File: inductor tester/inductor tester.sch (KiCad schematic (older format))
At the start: 39 parts, among them P101 I Sense, P102 Inductor Under Test, P103 V Sense, P104 10V_In, P105 0V_In, Q101 BC847, Q102 PSMN4R3-30BL, SW101 SW_PUSH, U102 LM555N

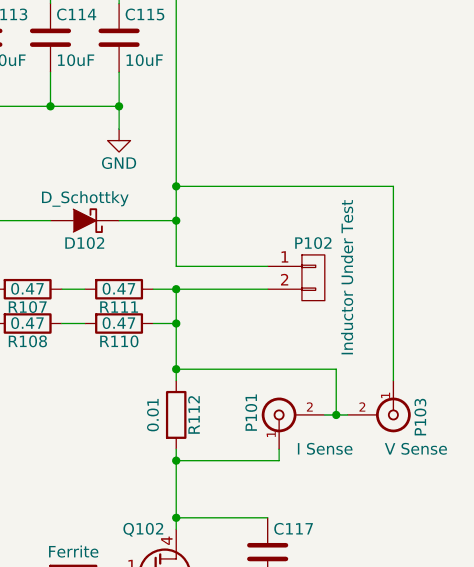
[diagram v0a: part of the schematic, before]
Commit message: Added notes on exporting, saved PCB as ordered.
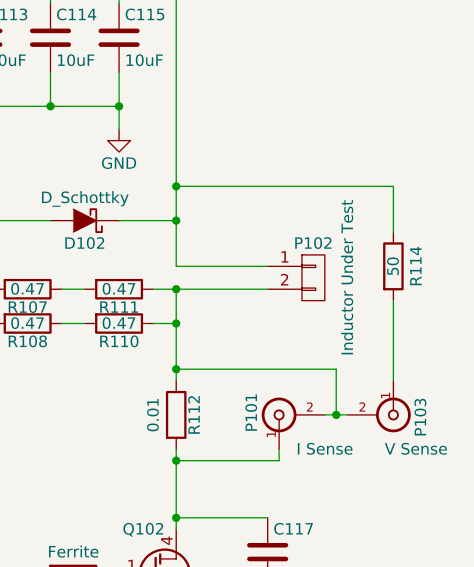
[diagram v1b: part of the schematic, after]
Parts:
- added R114: 50, Resistors_SMD:R_0805_HandSoldering, symbol R
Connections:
- net VCC: now also R114.1; no longer P103.1 (In)
- new net: P103.1 (In), R114.2
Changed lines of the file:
@@
 $EndComp
 $Comp
-L GND #PWR01
+L GND #PWR113
 U 1 1 571D57D3
 P 7350 5600
-F 0 "#PWR01" H 7350 5350 50  0001 C CNN
+F 0 "#PWR113" H 7350 5350 50  0001 C CNN
 F 1 "GND" H 7350 5450 50  0000 C CNN
 F 2 "" H 7350 5600 50  0000 C CNN
@@
 $EndComp
 $Comp
-L GND #PWR02
+L GND #PWR114
 U 1 1 571D8329
 P 8150 2800
-F 0 "#PWR02" H 8150 2550 50  0001 C CNN
+F 0 "#PWR114" H 8150 2550 50  0001 C CNN
 F 1 "GND" H 8150 2650 50  0000 C CNN
 F 2 "" H 8150 2800 50  0000 C CNN
@@
 $EndComp
 $Comp
-L GND #PWR03
+L GND #PWR102
 U 1 1 571DCF93
 P 4300 3800
-F 0 "#PWR03" H 4300 3550 50  0001 C CNN
+F 0 "#PWR102" H 4300 3550 50  0001 C CNN
 F 1 "GND" H 4300 3650 50  0000 C CNN
 F 2 "" H 4300 3800 50  0000 C CNN
@@
 $EndComp
 $Comp
-L GND #PWR04
+L GND #PWR110
 U 1 1 571DD8DF
 P 6500 5600
-F 0 "#PWR04" H 6500 5350 50  0001 C CNN
+F 0 "#PWR110" H 6500 5350 50  0001 C CNN
 F 1 "GND" H 6500 5450 50  0000 C CNN
 F 2 "" H 6500 5600 50  0000 C CNN
@@
 $EndComp
 $Comp
-L VCC #PWR05
+L VCC #PWR111
 U 1 1 571DF26F
 P 6950 3050
-F 0 "#PWR05" H 6950 2900 50  0001 C CNN
+F 0 "#PWR111" H 6950 2900 50  0001 C CNN
 F 1 "VCC" H 6950 3200 50  0000 C CNN
 F 2 "" H 6950 3050 50  0000 C CNN
@@
 $EndComp
 $Comp
-L VCC #PWR06
+L VCC #PWR107
 U 1 1 571DF3CD
 P 5150 3050
-F 0 "#PWR06" H 5150 2900 50  0001 C CNN
+F 0 "#PWR107" H 5150 2900 50  0001 C CNN
 F 1 "VCC" H 5150 3200 50  0000 C CNN
 F 2 "" H 5150 3050 50  0000 C CNN
@@
 $EndComp
 $Comp
-L VCC #PWR07
+L VCC #PWR105
 U 1 1 571DF44D
 P 4800 4600
-F 0 "#PWR07" H 4800 4450 50  0001 C CNN
+F 0 "#PWR105" H 4800 4450 50  0001 C CNN
 F 1 "VCC" H 4800 4750 50  0000 C CNN
 F 2 "" H 4800 4600 50  0000 C CNN
@@
 $EndComp
 $Comp
-L VCC #PWR08
+L VCC #PWR109
 U 1 1 571DF73B
 P 6500 4500
-F 0 "#PWR08" H 6500 4350 50  0001 C CNN
+F 0 "#PWR109" H 6500 4350 50  0001 C CNN
 F 1 "VCC" H 6500 4650 50  0000 C CNN
 F 2 "" H 6500 4500 50  0000 C CNN
@@
 Wire Wire Line
 	9100 3850 9100 4050
-Wire Wire Line
-	9350 3050 9350 3900
 Wire Wire Line
 	8800 4800 8800 4800
@@
 $EndComp
 $Comp
-L GND #PWR09
+L GND #PWR112
 U 1 1 571DFB52
 P 6950 4600
-F 0 "#PWR09" H 6950 4350 50  0001 C CNN
+F 0 "#PWR112" H 6950 4350 50  0001 C CNN
 F 1 "GND" H 6950 4450 50  0000 C CNN
 F 2 "" H 6950 4600 50  0000 C CNN
@@
 	5250 3850 5250 4000
 $Comp
-L GND #PWR010
+L GND #PWR108
 U 1 1 571E0244
 P 5250 4450
-F 0 "#PWR010" H 5250 4200 50  0001 C CNN
+F 0 "#PWR108" H 5250 4200 50  0001 C CNN
 F 1 "GND" H 5250 4300 50  0000 C CNN
 F 2 "" H 5250 4450 50  0000 C CNN
@@
 Pulse Width
 $Comp
-L GND #PWR011
+L GND #PWR106
 U 1 1 571E729D
 P 4800 5600
-F 0 "#PWR011" H 4800 5350 50  0001 C CNN
+F 0 "#PWR106" H 4800 5350 50  0001 C CNN
 F 1 "GND" H 4800 5450 50  0000 C CNN
 F 2 "" H 4800 5600 50  0000 C CNN
@@
 $EndComp
 $Comp
-L VCC #PWR012
+L VCC #PWR101
 U 1 1 571E79B0
 P 3950 2150
-F 0 "#PWR012" H 3950 2000 50  0001 C CNN
+F 0 "#PWR101" H 3950 2000 50  0001 C CNN
 F 1 "VCC" H 3950 2300 50  0000 C CNN
 F 2 "" H 3950 2150 50  0000 C CNN
@@
 $EndComp
 $Comp
-L VCC #PWR013
+L VCC #PWR103
 U 1 1 571E7BC6
 P 4300 4600
-F 0 "#PWR013" H 4300 4450 50  0001 C CNN
+F 0 "#PWR103" H 4300 4450 50  0001 C CNN
 F 1 "VCC" H 4300 4750 50  0000 C CNN
 F 2 "" H 4300 4600 50  0000 C CNN
@@
 $EndComp
 $Comp
-L GND #PWR014
+L GND #PWR104
 U 1 1 571E7C85
 P 4300 5200
-F 0 "#PWR014" H 4300 4950 50  0001 C CNN
+F 0 "#PWR104" H 4300 4950 50  0001 C CNN
 F 1 "GND" H 4300 5050 50  0000 C CNN
 F 2 "" H 4300 5200 50  0000 C CNN
@@
 Wire Wire Line
 	8000 3650 7900 3650
+$Comp
+L R R114
+U 1 1 5721D0F3
+P 9350 3400
+F 0 "R114" V 9450 3400 50  0000 C CNN
+F 1 "50" V 9350 3400 50  0000 C CNN
+F 2 "Resistors_SMD:R_0805_HandSoldering" V 9280 3400 50  0001 C CNN
+F 3 "" H 9350 3400 50  0000 C CNN
+	1    9350 3400
+	1    0    0    -1
+$EndComp
+Wire Wire Line
+	9350 3050 9350 3250
+Wire Wire Line
+	9350 3550 9350 3900
 $EndSCHEMATC

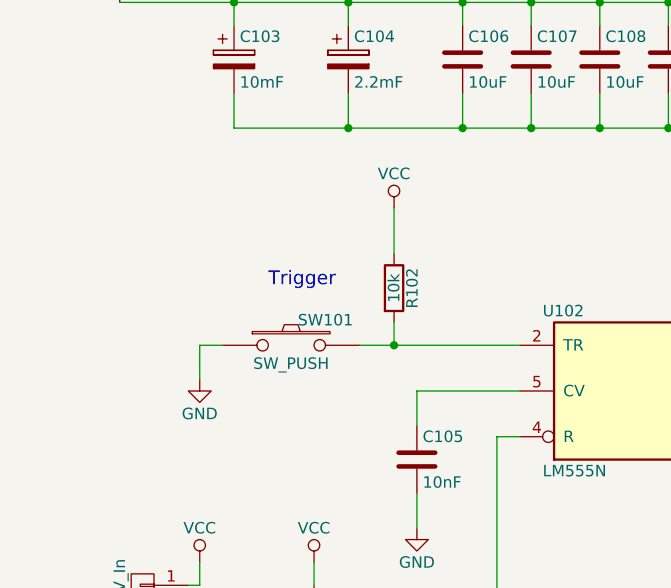
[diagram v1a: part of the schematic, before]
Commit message: PCB v2 - several changes:
  * Fixed reset issue that caused current limit oscillation
  * Switched 555 to an easier-to-solder footprint
  * Better silkscreen labelling
  * Improved BNC footprints to accept wider variety of connectors
  * Thermal relief for through hole pads
  * Added OSHW logo
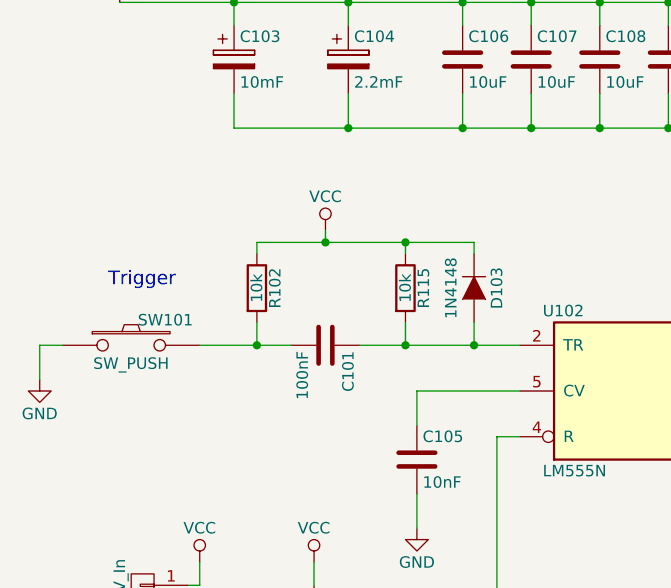
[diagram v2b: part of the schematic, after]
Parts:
- added C101: 100nF, Capacitors_SMD:C_0805_HandSoldering, symbol C
- added D103: 1N4148, Diodes_SMD:MiniMELF_Standard, symbol D
- added R115: 10k, Resistors_SMD:R_0805_HandSoldering, symbol R
- U102: footprint Housings_SSOP:TSSOP-8_4.4x3mm_Pitch0.65mm -> Housings_SOIC:SOIJ-8_5.3x5.3mm_Pitch1.27mm
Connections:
- net VCC: now also D103.1 (K), R115.1
- net at R102.2, SW101.2: now also C101.2; no longer U102.2 (TR)
- new net: C101.1, D103.2 (A), R115.2, U102.2 (TR)
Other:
- moved on the sheet: R102, SW101
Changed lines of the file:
@@
 $EndComp
 $Comp
-L GND #PWR113
+L GND #PWR01
 U 1 1 571D57D3
 P 7350 5600
-F 0 "#PWR113" H 7350 5350 50  0001 C CNN
+F 0 "#PWR01" H 7350 5350 50  0001 C CNN
 F 1 "GND" H 7350 5450 50  0000 C CNN
 F 2 "" H 7350 5600 50  0000 C CNN
@@
 F 0 "U102" H 5800 4200 50  0000 L CNN
 F 1 "LM555N" H 5800 3500 50  0000 L CNN
-F 2 "Housings_SSOP:TSSOP-8_4.4x3mm_Pitch0.65mm" H 6200 3850 50  0001 C CNN
+F 2 "Housings_SOIC:SOIJ-8_5.3x5.3mm_Pitch1.27mm" H 6200 3850 50  0001 C CNN
 F 3 "" H 6200 3850 50  0000 C CNN
 	1    6200 3850
@@
 $EndComp
 $Comp
-L GND #PWR114
+L GND #PWR02
 U 1 1 571D8329
 P 8150 2800
-F 0 "#PWR114" H 8150 2550 50  0001 C CNN
+F 0 "#PWR02" H 8150 2550 50  0001 C CNN
 F 1 "GND" H 8150 2650 50  0000 C CNN
 F 2 "" H 8150 2800 50  0000 C CNN
@@
 L R R102
 U 1 1 571DCF0A
-P 5150 3400
-F 0 "R102" V 5230 3400 50  0000 C CNN
-F 1 "10k" V 5150 3400 50  0000 C CNN
-F 2 "Resistors_SMD:R_0805_HandSoldering" V 5080 3400 50  0001 C CNN
-F 3 "" H 5150 3400 50  0000 C CNN
-	1    5150 3400
-	1    0    0    -1
-$EndComp
-$Comp
-L GND #PWR102
+P 4550 3400
+F 0 "R102" V 4630 3400 50  0000 C CNN
+F 1 "10k" V 4550 3400 50  0000 C CNN
+F 2 "Resistors_SMD:R_0805_HandSoldering" V 4480 3400 50  0001 C CNN
+F 3 "" H 4550 3400 50  0000 C CNN
+	1    4550 3400
+	1    0    0    -1
+$EndComp
+$Comp
+L GND #PWR03
 U 1 1 571DCF93
-P 4300 3800
-F 0 "#PWR102" H 4300 3550 50  0001 C CNN
-F 1 "GND" H 4300 3650 50  0000 C CNN
-F 2 "" H 4300 3800 50  0000 C CNN
-F 3 "" H 4300 3800 50  0000 C CNN
-	1    4300 3800
+P 3600 3800
+F 0 "#PWR03" H 3600 3550 50  0001 C CNN
+F 1 "GND" H 3600 3650 50  0000 C CNN
+F 2 "" H 3600 3800 50  0000 C CNN
+F 3 "" H 3600 3800 50  0000 C CNN
+	1    3600 3800
 	1    0    0    -1
 $EndComp
@@
 $EndComp
 $Comp
-L GND #PWR110
+L GND #PWR04
 U 1 1 571DD8DF
 P 6500 5600
-F 0 "#PWR110" H 6500 5350 50  0001 C CNN
+F 0 "#PWR04" H 6500 5350 50  0001 C CNN
 F 1 "GND" H 6500 5450 50  0000 C CNN
 F 2 "" H 6500 5600 50  0000 C CNN
@@
 $EndComp
 $Comp
-L VCC #PWR111
+L VCC #PWR05
 U 1 1 571DF26F
 P 6950 3050
-F 0 "#PWR111" H 6950 2900 50  0001 C CNN
+F 0 "#PWR05" H 6950 2900 50  0001 C CNN
 F 1 "VCC" H 6950 3200 50  0000 C CNN
 F 2 "" H 6950 3050 50  0000 C CNN
@@
 $EndComp
 $Comp
-L VCC #PWR107
+L VCC #PWR06
 U 1 1 571DF3CD
-P 5150 3050
-F 0 "#PWR107" H 5150 2900 50  0001 C CNN
-F 1 "VCC" H 5150 3200 50  0000 C CNN
-F 2 "" H 5150 3050 50  0000 C CNN
-F 3 "" H 5150 3050 50  0000 C CNN
-	1    5150 3050
-	1    0    0    -1
-$EndComp
-$Comp
-L VCC #PWR105
+P 4850 3150
+F 0 "#PWR06" H 4850 3000 50  0001 C CNN
+F 1 "VCC" H 4850 3300 50  0000 C CNN
+F 2 "" H 4850 3150 50  0000 C CNN
+F 3 "" H 4850 3150 50  0000 C CNN
+	1    4850 3150
+	1    0    0    -1
+$EndComp
+$Comp
+L VCC #PWR07
 U 1 1 571DF44D
 P 4800 4600
-F 0 "#PWR105" H 4800 4450 50  0001 C CNN
+F 0 "#PWR07" H 4800 4450 50  0001 C CNN
 F 1 "VCC" H 4800 4750 50  0000 C CNN
 F 2 "" H 4800 4600 50  0000 C CNN
@@
 $EndComp
 $Comp
-L VCC #PWR109
+L VCC #PWR08
 U 1 1 571DF73B
 P 6500 4500
-F 0 "#PWR109" H 6500 4350 50  0001 C CNN
+F 0 "#PWR08" H 6500 4350 50  0001 C CNN
 F 1 "VCC" H 6500 4650 50  0000 C CNN
 F 2 "" H 6500 4500 50  0000 C CNN
@@
 	6950 4050 6700 4050
 Wire Wire Line
-	4300 3800 4300 3650
-Wire Wire Line
-	4300 3650 4400 3650
-Wire Wire Line
-	5000 3650 5700 3650
-Wire Wire Line
-	5150 3650 5150 3550
-Connection ~ 5150 3650
+	3600 3800 3600 3650
+Wire Wire Line
+	3600 3650 3700 3650
+Wire Wire Line
+	4300 3650 4700 3650
+Wire Wire Line
+	4550 3650 4550 3550
+Connection ~ 4550 3650
 Wire Wire Line
 	6950 3050 6950 3100
@@
 $EndComp
 $Comp
-L GND #PWR112
+L GND #PWR09
 U 1 1 571DFB52
 P 6950 4600
-F 0 "#PWR112" H 6950 4350 50  0001 C CNN
+F 0 "#PWR09" H 6950 4350 50  0001 C CNN
 F 1 "GND" H 6950 4450 50  0000 C CNN
 F 2 "" H 6950 4600 50  0000 C CNN
@@
 Connection ~ 6950 3850
 Connection ~ 6950 4050
-Wire Wire Line
-	5150 3050 5150 3250
 $Comp
 L C C105
@@
 	5250 3850 5250 4000
 $Comp
-L GND #PWR108
+L GND #PWR010
 U 1 1 571E0244
 P 5250 4450
-F 0 "#PWR108" H 5250 4200 50  0001 C CNN
+F 0 "#PWR010" H 5250 4200 50  0001 C CNN
 F 1 "GND" H 5250 4300 50  0000 C CNN
 F 2 "" H 5250 4450 50  0000 C CNN
@@
 Text Notes 6650 5350 0    60   ~ 0
 Current limit
-Text Notes 4600 3400 0    60   ~ 0
+Text Notes 3900 3400 0    60   ~ 0
 Trigger
 Text Notes 7150 3550 3    60   ~ 0
 Pulse Width
 $Comp
-L GND #PWR106
+L GND #PWR011
 U 1 1 571E729D
 P 4800 5600
-F 0 "#PWR106" H 4800 5350 50  0001 C CNN
+F 0 "#PWR011" H 4800 5350 50  0001 C CNN
 F 1 "GND" H 4800 5450 50  0000 C CNN
 F 2 "" H 4800 5600 50  0000 C CNN
@@
 $EndComp
 $Comp
-L VCC #PWR101
+L VCC #PWR012
 U 1 1 571E79B0
 P 3950 2150
-F 0 "#PWR101" H 3950 2000 50  0001 C CNN
+F 0 "#PWR012" H 3950 2000 50  0001 C CNN
 F 1 "VCC" H 3950 2300 50  0000 C CNN
 F 2 "" H 3950 2150 50  0000 C CNN
@@
 $EndComp
 $Comp
-L VCC #PWR103
+L VCC #PWR013
 U 1 1 571E7BC6
 P 4300 4600
-F 0 "#PWR103" H 4300 4450 50  0001 C CNN
+F 0 "#PWR013" H 4300 4450 50  0001 C CNN
 F 1 "VCC" H 4300 4750 50  0000 C CNN
 F 2 "" H 4300 4600 50  0000 C CNN
@@
 $EndComp
 $Comp
-L GND #PWR104
+L GND #PWR014
 U 1 1 571E7C85
 P 4300 5200
-F 0 "#PWR104" H 4300 4950 50  0001 C CNN
+F 0 "#PWR014" H 4300 4950 50  0001 C CNN
 F 1 "GND" H 4300 5050 50  0000 C CNN
 F 2 "" H 4300 5200 50  0000 C CNN
@@
 L SW_PUSH SW101
 U 1 1 571E9617
-P 4700 3650
-F 0 "SW101" H 4850 3760 50  0000 C CNN
-F 1 "SW_PUSH" H 4700 3570 50  0000 C CNN
-F 2 "momentary_button:momentary_tactile_6x6x4" H 4700 3650 50  0001 C CNN
-F 3 "" H 4700 3650 50  0000 C CNN
-	1    4700 3650
+P 4000 3650
+F 0 "SW101" H 4150 3760 50  0000 C CNN
+F 1 "SW_PUSH" H 4000 3570 50  0000 C CNN
+F 2 "momentary_button:momentary_tactile_6x6x4" H 4000 3650 50  0001 C CNN
+F 3 "" H 4000 3650 50  0000 C CNN
+	1    4000 3650
 	1    0    0    -1
 $EndComp
@@
 Wire Wire Line
 	9350 3550 9350 3900
+$Comp
+L C C101
+U 1 1 574BFB7A
+P 4850 3650
+F 0 "C101" H 4875 3750 50  0000 L CNN
+F 1 "100nF" H 4875 3550 50  0000 L CNN
+F 2 "Capacitors_SMD:C_0805_HandSoldering" H 4888 3500 50  0001 C CNN
+F 3 "" H 4850 3650 50  0000 C CNN
+	1    4850 3650
+	0    1    1    0
+$EndComp
+Wire Wire Line
+	5000 3650 5700 3650
+$Comp
+L R R115
+U 1 1 574BFDAE
+P 5200 3400
+F 0 "R115" V 5280 3400 50  0000 C CNN
+F 1 "10k" V 5200 3400 50  0000 C CNN
+F 2 "Resistors_SMD:R_0805_HandSoldering" V 5130 3400 50  0001 C CNN
+F 3 "" H 5200 3400 50  0000 C CNN
+	1    5200 3400
+	1    0    0    -1
+$EndComp
+Wire Wire Line
+	5200 3550 5200 3650
+Connection ~ 5200 3650
+$Comp
+L D D103
+U 1 1 574C01DF
+P 5500 3400
+F 0 "D103" H 5500 3500 50  0000 C CNN
+F 1 "1N4148" H 5500 3300 50  0000 C CNN
+F 2 "Diodes_SMD:MiniMELF_Standard" H 5500 3400 50  0001 C CNN
+F 3 "" H 5500 3400 50  0000 C CNN
+	1    5500 3400
+	0    1    1    0
+$EndComp
+Wire Wire Line
+	5500 3550 5500 3650
+Connection ~ 5500 3650
+Wire Wire Line
+	5500 3200 5500 3250
+Wire Wire Line
+	4550 3200 5500 3200
+Wire Wire Line
+	4850 3200 4850 3150
+Wire Wire Line
+	5200 3250 5200 3200
+Connection ~ 5200 3200
+Wire Wire Line
+	4550 3200 4550 3250
+Connection ~ 4850 3200
 $EndSCHEMATC
